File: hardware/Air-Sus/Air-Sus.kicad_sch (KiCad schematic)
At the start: 31 parts, among them IC1 ABPMRRV060MG2A3, J1 53307-2471, J3 Conn_01x04, J4 MX150_02x08_Vertical, J6 PeripheralCAN, U1 VL53L0CXV0DH1

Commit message: finished schematic for all
Signed-off-by: Vortex-Overdrive <kkurapati10@gmail.com>
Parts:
- removed C5: 10uf, symbol Device:C
- removed C6: 0.1uf, symbol Device:C
- removed J4: MX150_02x08_Vertical, UTSVT_Connectors:CONN16_0757575481_MOL, symbol utsvt_connectors:MX150_02x08_Vertical
- removed R13, R4, R5, R8: 10k, symbol Device:R
- removed U1: VL53L0CXV0DH1, Sensor_Distance:ST_VL53L1x, symbol Sensor_Distance:VL53L0CXV0DH1
- added J2, J4: Conn_01x05, symbol Connector_Generic:Conn_01x05
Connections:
- net LED_3v is gone; now on net +3.3V: R11.1
- net pressure_error is gone; now on net pressure_err: TP5.1
- net +3.3V: now also J2.3 (Pin_3), J4.5 (Pin_5)
- net GND: now also J2.1 (Pin_1), J4.2 (Pin_2)
- net SCL: now also J2.4 (Pin_4), J4.4 (Pin_4)
- net SDA: now also J2.2 (Pin_2), J4.3 (Pin_3)
- net GPIO1: now reaches J1.11 (ADC1_IN9)
- net GPIO1: now also J2.5 (Pin_5)
- no-connect marks 4 -> 15
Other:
- moved on the sheet: D1, D2, D3, R10, R11, R12, TP1, TP2, TP3, TP4, TP5, TP6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

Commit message: small changes
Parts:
- added GND_TP2: TestPoint, symbol Connector:TestPoint
- R10, R11, R12: value R -> 100
- R3: value 10k -> 4.7k
- renumbered TP6 to GNDA_TP1, TP2 to GND_TP1, TP7 to GND_TP3, TP1 to LinPot_TP, TP5 to PressureErr_TP, TP3 to SCL_TP, TP4 to SDA_TP
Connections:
- net +3.3V: no longer J3.4 (Pin_4)
- net GND: now also GND_TP2.1; no longer D3.1 (K)
- net GNDA: now also D3.1 (K)
- net VDDA: now also J3.4 (Pin_4)
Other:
- note added: "resistor to limit current if placed in reverse"
- moved on the sheet: GND_TP3, J4, SDA_TP

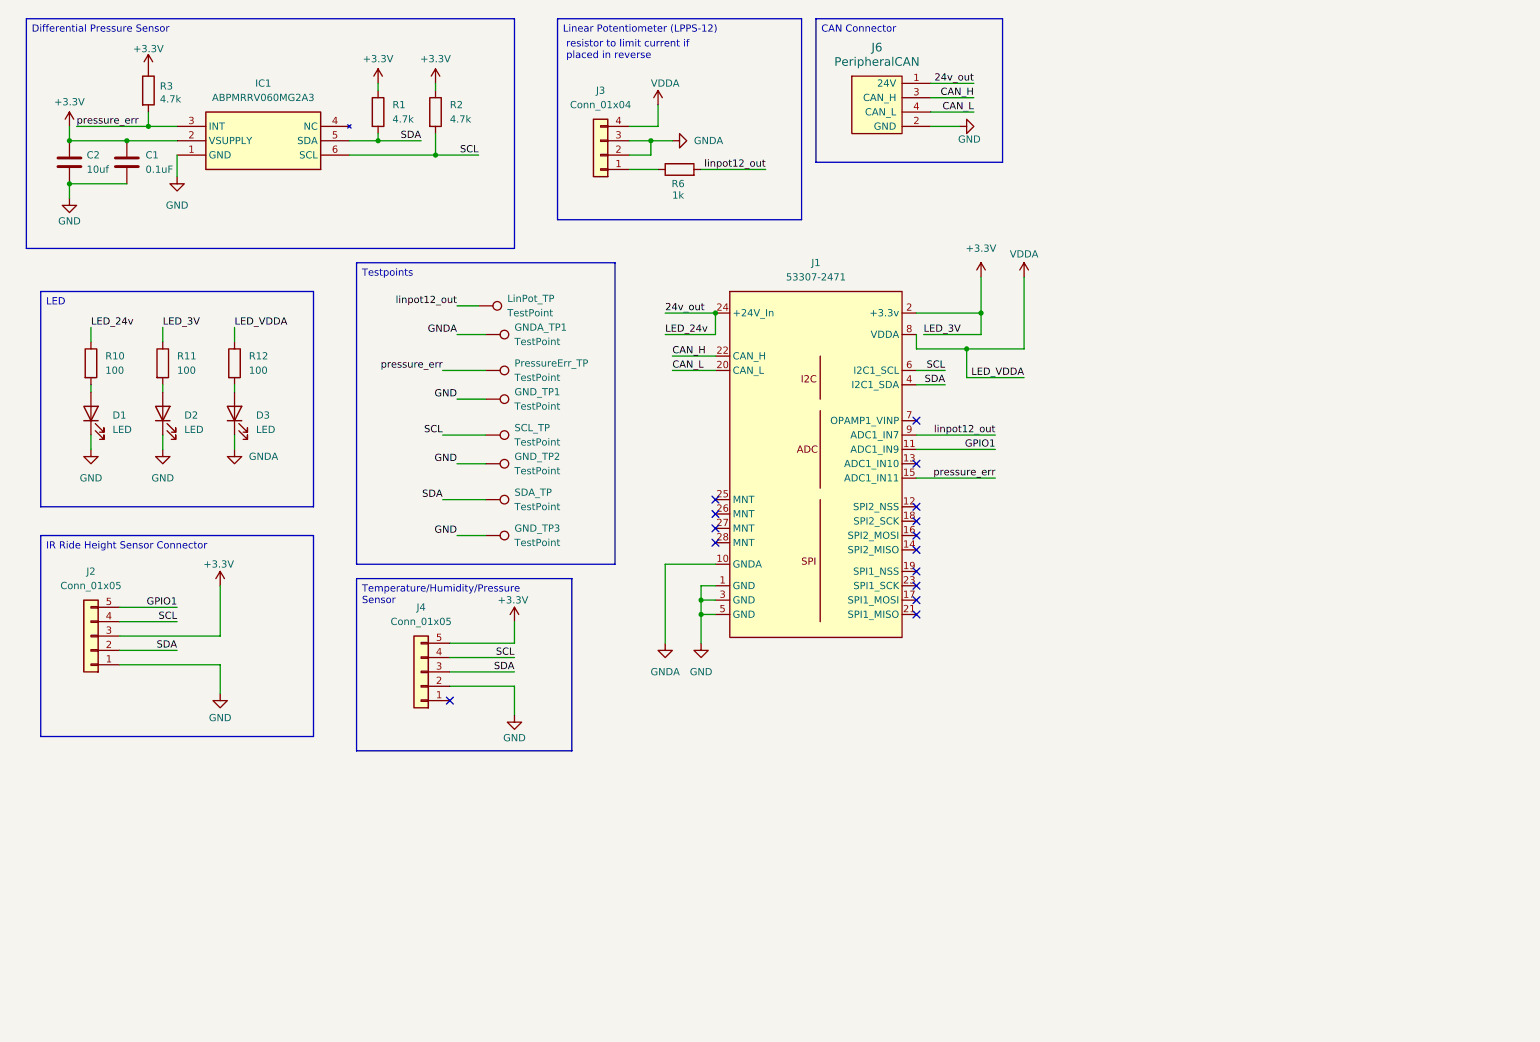
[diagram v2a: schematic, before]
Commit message: added op-amp, finished footprints, new connector, fuse, ldo
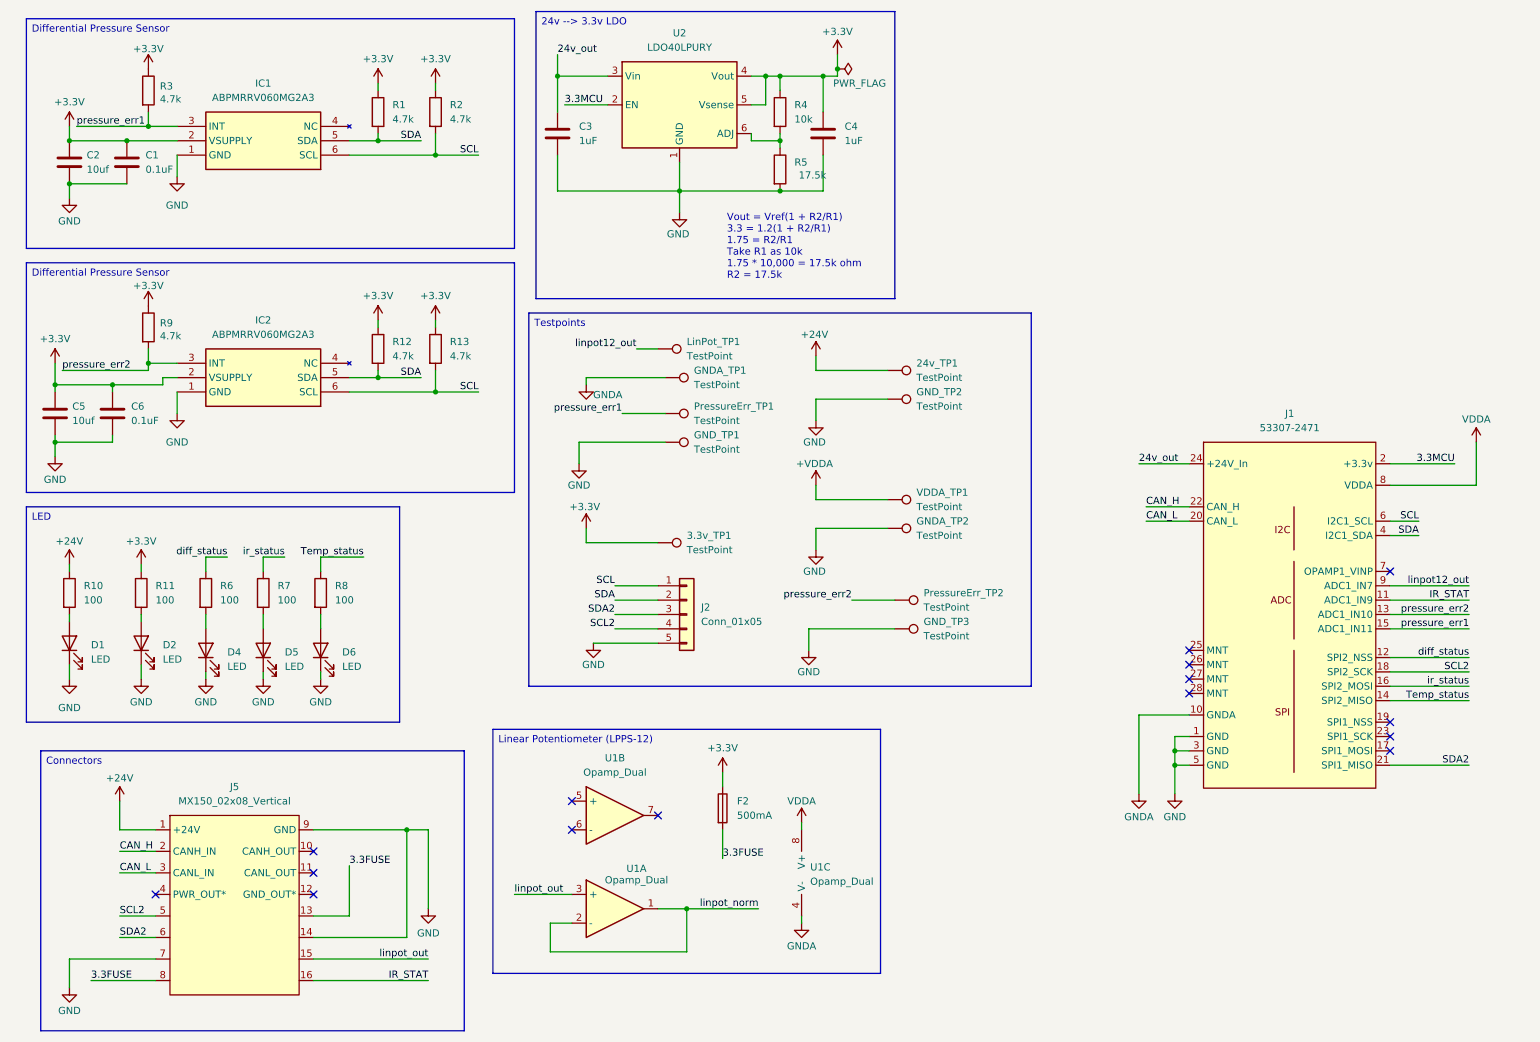
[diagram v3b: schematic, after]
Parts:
- removed D3: LED, symbol Device:LED
- removed J3: Conn_01x04, symbol Connector_Generic:Conn_01x04
- removed J4: Conn_01x05, symbol Connector_Generic:Conn_01x05
- removed J6: PeripheralCAN, UTSVT_Connectors:Molex_Nano-Fit_105309-xx04_1x04_P2.50mm_Vertical, symbol utsvt_connectors:PeripheralCANConnector
- removed SCL_TP, SDA_TP: TestPoint, symbol Connector:TestPoint
- added 24v_TP1, 3.3v_TP1, GNDA_TP2, PressureErr_TP2, VDDA_TP1: TestPoint, TestPoint:TestPoint_Pad_1.0x1.0mm, symbol Connector:TestPoint
- added C3, C4: 1uF, Capacitor_SMD:C_0603_1608Metric_Pad1.08x0.95mm_HandSolder, symbol Device:C
- added C5: 10uf, Capacitor_SMD:C_0603_1608Metric_Pad1.08x0.95mm_HandSolder, symbol Device:C
- added C6: 0.1uF, Capacitor_SMD:C_0603_1608Metric_Pad1.08x0.95mm_HandSolder, symbol Device:C
- added D4, D5, D6: LED, Capacitor_SMD:C_0603_1608Metric_Pad1.08x0.95mm_HandSolder, symbol Device:LED
- added F2: 500mA, Fuse:Fuseholder_Blade_Mini_Keystone_3568, symbol Device:Fuse
- added IC2: ABPMRRV060MG2A3, footprints:ABPMRRV060MG2A3, symbol ABPMRRV060MG2A3:ABPMRRV060MG2A3
- added J5: MX150_02x08_Vertical, UTSVT_Connectors:CONN16_0757575481_MOL, symbol utsvt_connectors:MX150_02x08_Vertical
- added R13, R9: 4.7k, Resistor_SMD:R_0603_1608Metric_Pad0.98x0.95mm_HandSolder, symbol Device:R
- added R4: 10k, Resistor_SMD:R_0603_1608Metric_Pad0.98x0.95mm_HandSolder, symbol Device:R
- added R5: 17.5k, Resistor_SMD:R_0603_1608Metric_Pad0.98x0.95mm_HandSolder, symbol Device:R
- added R7, R8: 100, Resistor_SMD:R_0603_1608Metric_Pad0.98x0.95mm_HandSolder, symbol Device:R
- added U1: Opamp_Dual, TLV900QDRQ1:SOIC8_D_TEX, symbol Device:Opamp_Dual
- added U2: LDO40LPURY, Package_DFN_QFN:DFN-6-1EP_3x3mm_P0.95mm_EP1.7x2.6mm, symbol Regulator_Linear:LDO40LPURY
- C1, D1, D2: footprint (none) -> Capacitor_SMD:C_0603_1608Metric_Pad1.08x0.95mm_HandSolder
- C2: footprint (none) -> Capacitor_SMD:C_0805_2012Metric
- GNDA_TP1, GND_TP1, GND_TP2, GND_TP3: footprint (none) -> TestPoint:TestPoint_Pad_1.0x1.0mm
- IC1: footprint ABPMRRV060MG2A3 -> footprints:ABPMRRV060MG2A3
- J2: footprint (none) -> Connector_PinHeader_2.54mm:PinHeader_1x05_P2.54mm_Vertical
- LinPot_TP1: renamed from LinPot_TP; footprint (none) -> TestPoint:TestPoint_Pad_1.0x1.0mm
- PressureErr_TP1: renamed from PressureErr_TP; footprint (none) -> TestPoint:TestPoint_Pad_1.0x1.0mm
- R1, R10, R11, R2, R3: footprint (none) -> Resistor_SMD:R_0603_1608Metric_Pad0.98x0.95mm_HandSolder
- R12: value 100 -> 4.7k; footprint (none) -> Resistor_SMD:R_0603_1608Metric_Pad0.98x0.95mm_HandSolder
- R6: value 1k -> 100; footprint (none) -> Resistor_SMD:R_0603_1608Metric_Pad0.98x0.95mm_HandSolder
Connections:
- net +3.3V: now also R12.1, 3.3v_TP1.1, C4.1, C5.1, C6.1, F2.1, IC2.2 (VSUPPLY), R13.1, R4.1, R9.1, U2.4 (Vout), U2.5 (Vsense); no longer J1.2 (+3.3v), J2.3 (Pin_3)
- net 24v_out: now also C3.1, U2.3 (Vin); no longer R10.1
- net CAN_H: now also J5.2 (CANH_IN)
- net CAN_L: now also J5.3 (CANL_IN)
- net GND: now also J2.5 (Pin_5), C3.2, C4.2, C5.2, C6.2, D4.1 (K), D5.1 (K), D6.1 (K), GNDA_TP2.1, IC2.1 (GND), J5.14, J5.7, J5.9 (GND), R5.2, U2.1 (GND), U2.7 (GND); no longer J2.1 (Pin_1)
- net GNDA: now also U1.4 (V-)
- net SCL: now also J2.1 (Pin_1), IC2.6 (SCL), R13.2; no longer J2.4 (Pin_4)
- net SDA: now also R12.2, IC2.5 (SDA)
- net VDDA: now also U1.8 (V+); no longer R12.1
- net linpot12_out: no longer R6.2
- net diff_status: now reaches J1.12 (SPI2_NSS)
- net diff_status: now also R6.1
- net pressure_err2: now reaches J1.13 (ADC1_IN10)
- net pressure_err2: now also IC2.3 (INT), PressureErr_TP2.1, R9.2
- net Temp_status: now reaches J1.14 (SPI2_MISO)
- net Temp_status: now also R8.1
- net ir_status: now reaches J1.16 (SPI2_MOSI)
- net ir_status: now also R7.1
- net SCL2: now reaches J1.18 (SPI2_SCK)
- net SCL2: now also J2.4 (Pin_4), J5.5
- net SDA2: now reaches J1.21 (SPI1_MISO)
- net SDA2: now also J2.3 (Pin_3), J5.6
- net GPIO1 renamed IR_STAT
- net IR_STAT: now also J5.16; no longer J2.5 (Pin_5)
- net pressure_err renamed pressure_err1
- new net: R4.2, R5.1, U2.6 (ADJ)
- new net: D6.2 (A), R8.2
- new net: D5.2 (A), R7.2
- new net: D4.2 (A), R6.2
- new net +24V: 24v_TP1.1, J5.1 (+24V), R10.1
- new net +VDDA: VDDA_TP1.1
- new net 3.3FUSE: F2.2, J5.13, J5.8
- new net 3.3MCU: J1.2 (+3.3v), U2.2 (EN)
- new net linpot_norm: U1.1, U1.2 (-)
- new net linpot_out: J5.15, U1.3 (+)
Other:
- note added: "Vout = Vref(1 + R2/R1) 3.3 = 1.2(1 + R2/R1) 1.75 = R2/R1 Take R1 as 10k 1.75 * 10,000 = 17.5k ohm R2 = 17.5k"
- note removed: "resistor to limit current if placed in reverse"
- moved on the sheet: D1, D2, GNDA_TP1, GND_TP1, J1, LinPot_TP1, PressureErr_TP1, R10, R11

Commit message: added configurable options for board type/connector, cubemx ioc, nanofit for ir rideheight, added part numbers, etc.
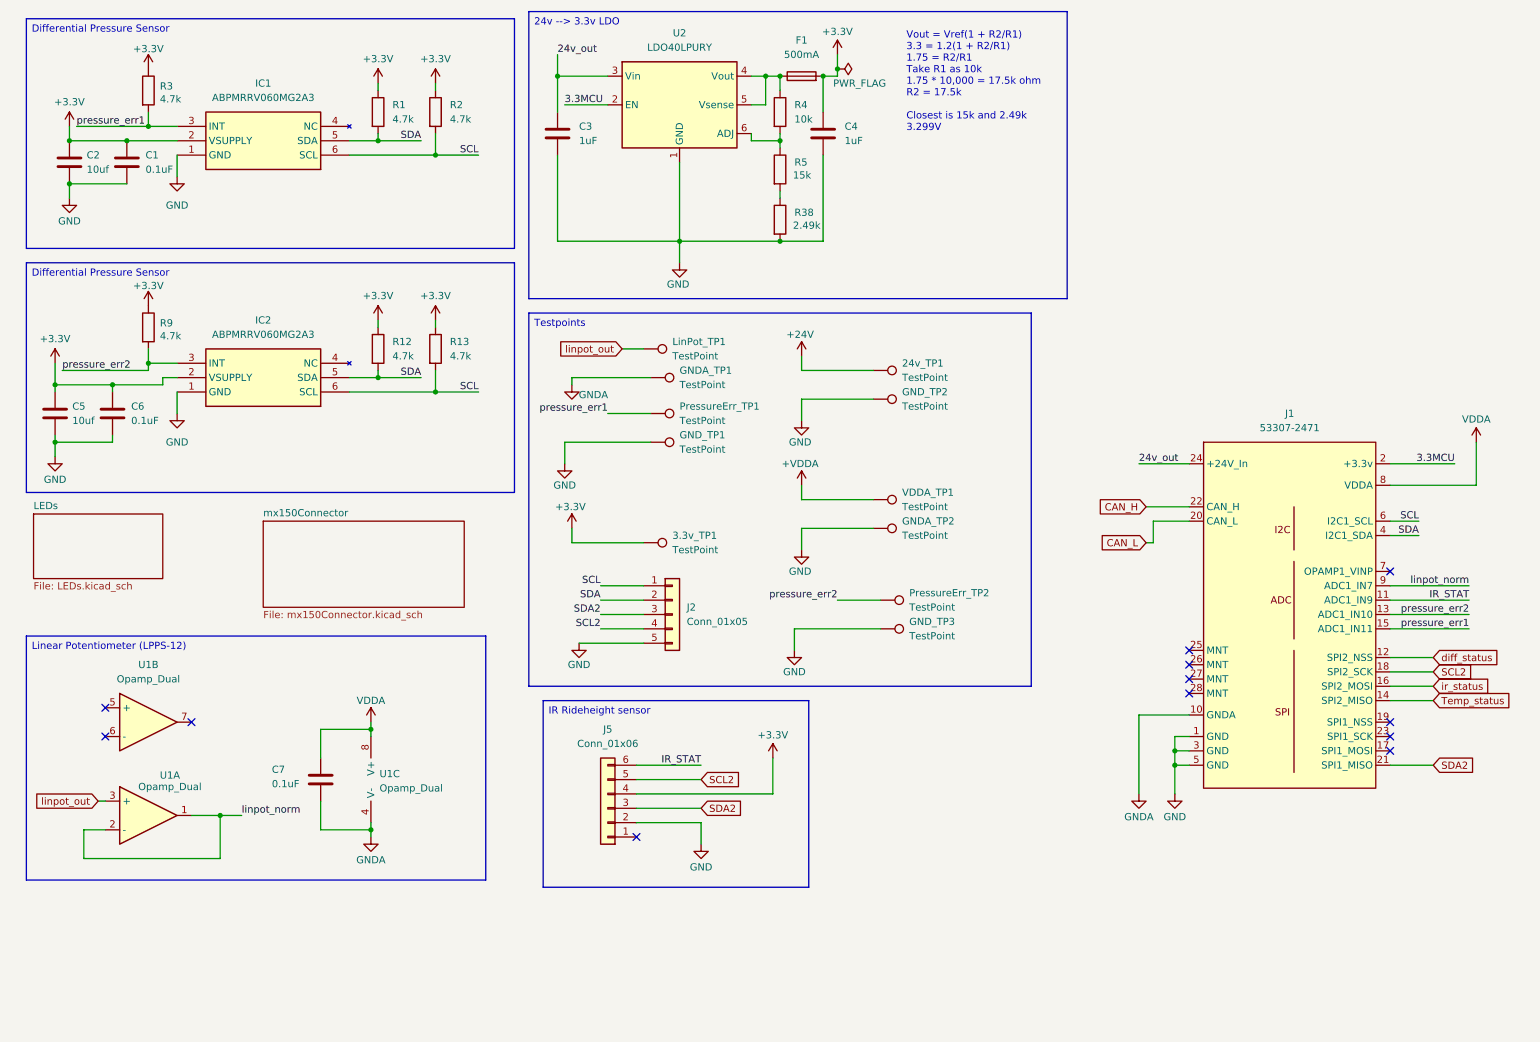
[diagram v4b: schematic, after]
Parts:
- removed D1, D2, D4, D5, D6: LED, Capacitor_SMD:C_0603_1608Metric_Pad1.08x0.95mm_HandSolder, symbol Device:LED
- removed F2: 500mA, Fuse:Fuseholder_Blade_Mini_Keystone_3568, symbol Device:Fuse
- removed J5: MX150_02x08_Vertical, UTSVT_Connectors:CONN16_0757575481_MOL, symbol utsvt_connectors:MX150_02x08_Vertical
- removed R10, R11, R6, R7, R8: 100, Resistor_SMD:R_0603_1608Metric_Pad0.98x0.95mm_HandSolder, symbol Device:R
- added C7: 0.1uF, Capacitor_SMD:C_0603_1608Metric_Pad1.08x0.95mm_HandSolder, symbol Device:C
- added F1: 500mA, Fuse:Fuseholder_Blade_Mini_Keystone_3568, symbol Device:Fuse
- added J5: Conn_01x06, Connector_Molex:Molex_Nano-Fit_105310-xx06_2x03_P2.50mm_Vertical, symbol Connector_Generic:Conn_01x06
- added R38: 2.49k, Resistor_SMD:R_0603_1608Metric_Pad0.98x0.95mm_HandSolder, symbol Device:R
- C1, C6: P/N (none) -> C14663
- C2, C5: P/N (none) -> C440198
- C3, C4: P/N (none) -> C15849
- IC1, IC2: P/N (none) -> 785-ABPMRRV060MG2A3
- R1, R12, R13, R2, R3, R9: P/N (none) -> 71-CRCW0603-4.7K-E3
- R4: P/N (none) -> C25804
- R5: value 17.5k -> 15k; P/N (none) -> C22809
- U1: P/N (none) -> 595-TLV9002QDRQ1
- U2: P/N (none) -> 511-LDO40LPU33RY
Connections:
- net +3.3V: now also F1.2, J5.4 (Pin_4); no longer R4.1, U2.4 (Vout), U2.5 (Vsense)
- net GND: now also J5.2 (Pin_2), R38.2; no longer R5.2
- net GNDA: now also C7.2
- net IR_STAT: now also J5.6 (Pin_6)
- net SCL2: now also J5.5 (Pin_5)
- net SDA2: now also J5.3 (Pin_3)
- net VDDA: now also C7.1
- net linpot_norm: now also J1.9 (ADC1_IN7)
- net linpot_out: now also LinPot_TP1.1
- removed net linpot12_out: J1.9 (ADC1_IN7), LinPot_TP1.1
- new net: R38.1, R5.2
- new net: F1.1, R4.1, U2.4 (Vout), U2.5 (Vsense)
- no-connect marks 15 -> 12
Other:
- added sheet LEDs (LEDs.kicad_sch)
- added sheet mx150Connector (mx150Connector.kicad_sch)
- note added: "Vout = Vref(1 + R2/R1) 3.3 = 1.2(1 + R2/R1) 1.75 = R2/R1 Take R1 as 10k 1.75 * 10,000 = 17.5k ohm R2 = 17.5k Closest is 15k and 2.49k 3.299V"
- note removed: "Vout = Vref(1 + R2/R1) 3.3 = 1.2(1 + R2/R1) 1.75 = R2/R1 Take R1 as 10k 1.75 * 10,000 = 17.5k ohm R2 = 17.5k"
- moved on the sheet: 24v_TP1, 3.3v_TP1, GNDA_TP1, GNDA_TP2, GND_TP1, GND_TP2, GND_TP3, J2, LinPot_TP1, PressureErr_TP1, PressureErr_TP2, U1A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

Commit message: air-sus layout check e Please enter the commit message for your changes. Lines starting
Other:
- moved on the sheet: C7, U1A, U1B, U1C

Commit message: finished rev a layout for all 3 boards + added cubemx file
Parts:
- removed C1, C6: 0.1uF, Capacitor_SMD:C_0603_1608Metric_Pad1.08x0.95mm_HandSolder, symbol Device:C
- removed C2: 10uf, Capacitor_SMD:C_0805_2012Metric, symbol Device:C
- removed C5: 10uf, Capacitor_SMD:C_0603_1608Metric_Pad1.08x0.95mm_HandSolder, symbol Device:C
- removed IC1, IC2: ABPMRRV060MG2A3, footprints:ABPMRRV060MG2A3, symbol ABPMRRV060MG2A3:ABPMRRV060MG2A3
- removed R1, R12, R13, R2, R3, R9: 4.7k, Resistor_SMD:R_0603_1608Metric_Pad0.98x0.95mm_HandSolder, symbol Device:R
- C3, C4: P/N C15849 -> MLASU168SB5105KTNA01
- C7: P/N C14663 -> MLASU168SB5105KTNA01
- R38: P/N C2930072 -> CRCW06032K49FKEAC
- R4: P/N C25804 -> CRCW060310K0FKEI
- R5: P/N C22809 -> CRCW060315K0FKEA
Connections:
- net +VDDA is gone; now on net VDDA: VDDA_TP1.1
- net 24v_out: now also U2.2 (EN)
- net SCL: now also J5.5 (Pin_5)
- net SCL2: no longer J5.5 (Pin_5)
- net SDA: now also J5.3 (Pin_3)
- net SDA2: now also J1.14 (SPI2_MISO); no longer J1.21 (SPI1_MISO), J5.3 (Pin_3)
- net Temp_status: now also J1.7 (OPAMP1_VINP); no longer J1.14 (SPI2_MISO)
- net pressure_err1: now also J1.23 (SPI1_SCK); no longer J1.15 (ADC1_IN11)
- net pressure_err2: now also J1.11 (ADC1_IN9); no longer J1.13 (ADC1_IN10)
- net IR_INTER: now reaches J1.19 (SPI1_NSS)
- net IR_INTER: now also J5.6 (Pin_6)
- net 3.3MCU renamed +3.3V MCU
- net +3.3V MCU: no longer U2.2 (EN)
- removed net IR_STAT: J1.11 (ADC1_IN9), J5.6 (Pin_6)
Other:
- added sheet Differential Pressure Sensor1 (diffpress.kicad_sch)
- added sheet Differential Pressure Sensor2 (diffpress.kicad_sch)
- sheet LEDs ports: added Diff_Status, Temp_status, ir_status; removed none
- sheet mx150Connector ports: added CAN_H, CAN_L, SCL, SCL2, SDA, SDA2, linpot_out; removed none
- moved on the sheet: J5

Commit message: relayout
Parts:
- removed C7: 0.1uF, Capacitor_SMD:C_0603_1608Metric_Pad1.08x0.95mm_HandSolder, symbol Device:C
- removed U1: Opamp_Dual, TLV900QDRQ1:SOIC8_D_TEX, symbol Device:Opamp_Dual
- added C10: 0.1uF, Capacitor_SMD:C_0603_1608Metric_Pad1.08x0.95mm_HandSolder, symbol Device:C
- added U3: TLV9002QDRQ1, Air-Sus Footprints:SOIC8_D_TEX, symbol TLV9002QDRQ1:TLV9002QDRQ1
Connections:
- net GNDA: now also C10.2, U3.7 (V-)
- net VDDA: now also C10.1, U3.8 (V+)
- net linpot_norm: now also U3.1 (IN1-), U3.5 (OUT1)
- net linpot_out: now also U3.2 (IN1+)
